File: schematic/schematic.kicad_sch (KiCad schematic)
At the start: 19 parts, among them Q3 2N7000, SW1 PAIRING, U1 MCP4161-xxxx-P, U2 MCP4161-xxxx-P, U3 ESP32-WROOM-32E, U4 MCP4161-xxxx-P, U5 MCP4161-xxxx-P, U6 74HCT245

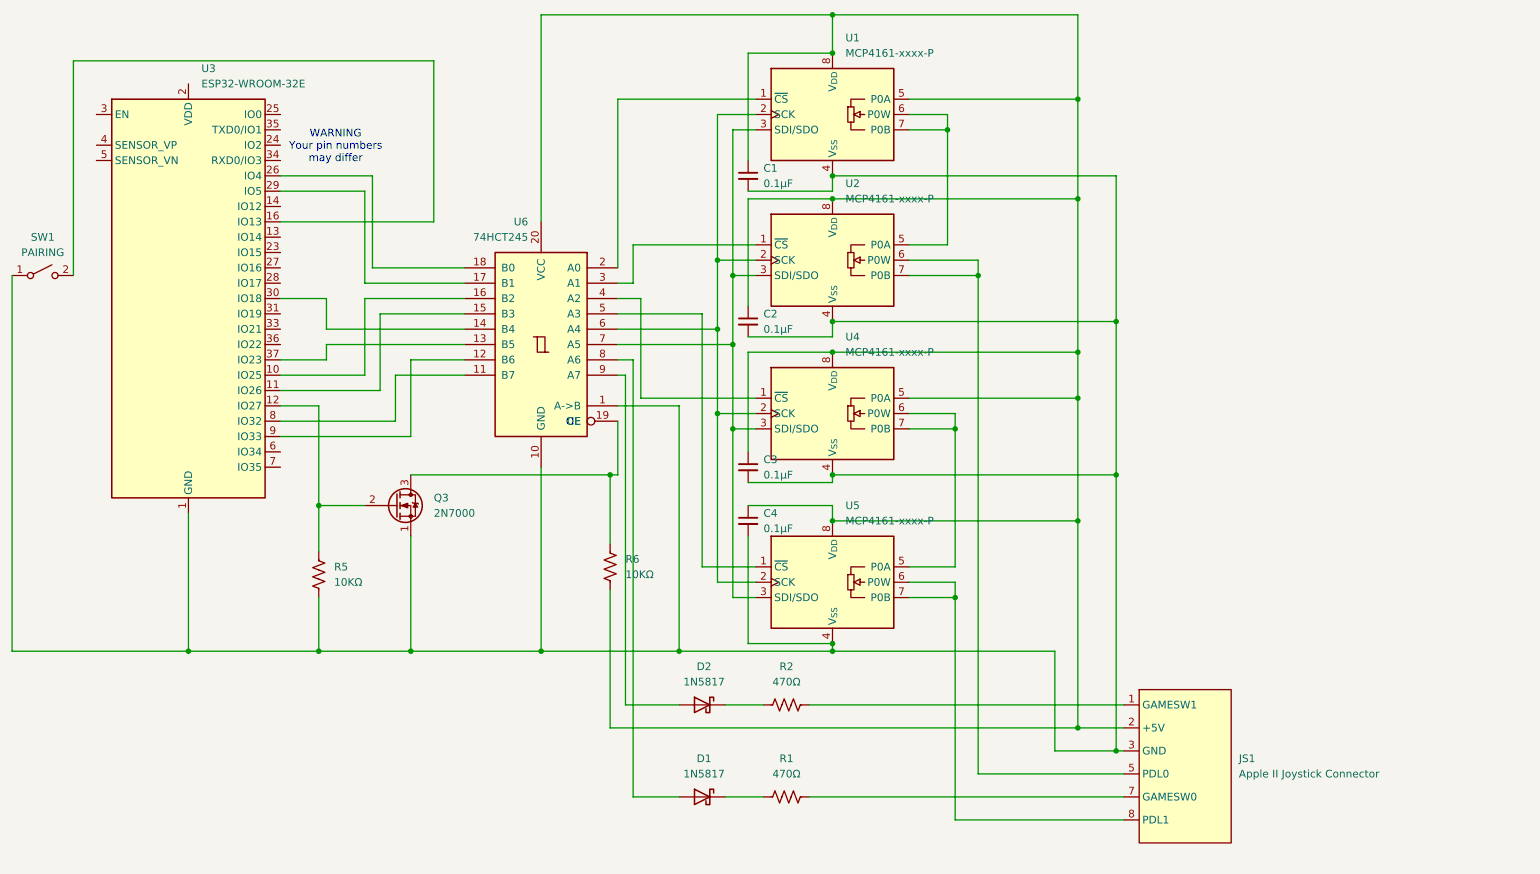
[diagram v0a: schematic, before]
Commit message: pcb first draft
minor changes to the schematic: DE9 connector symbol, the 2 separate diodes changed to one component
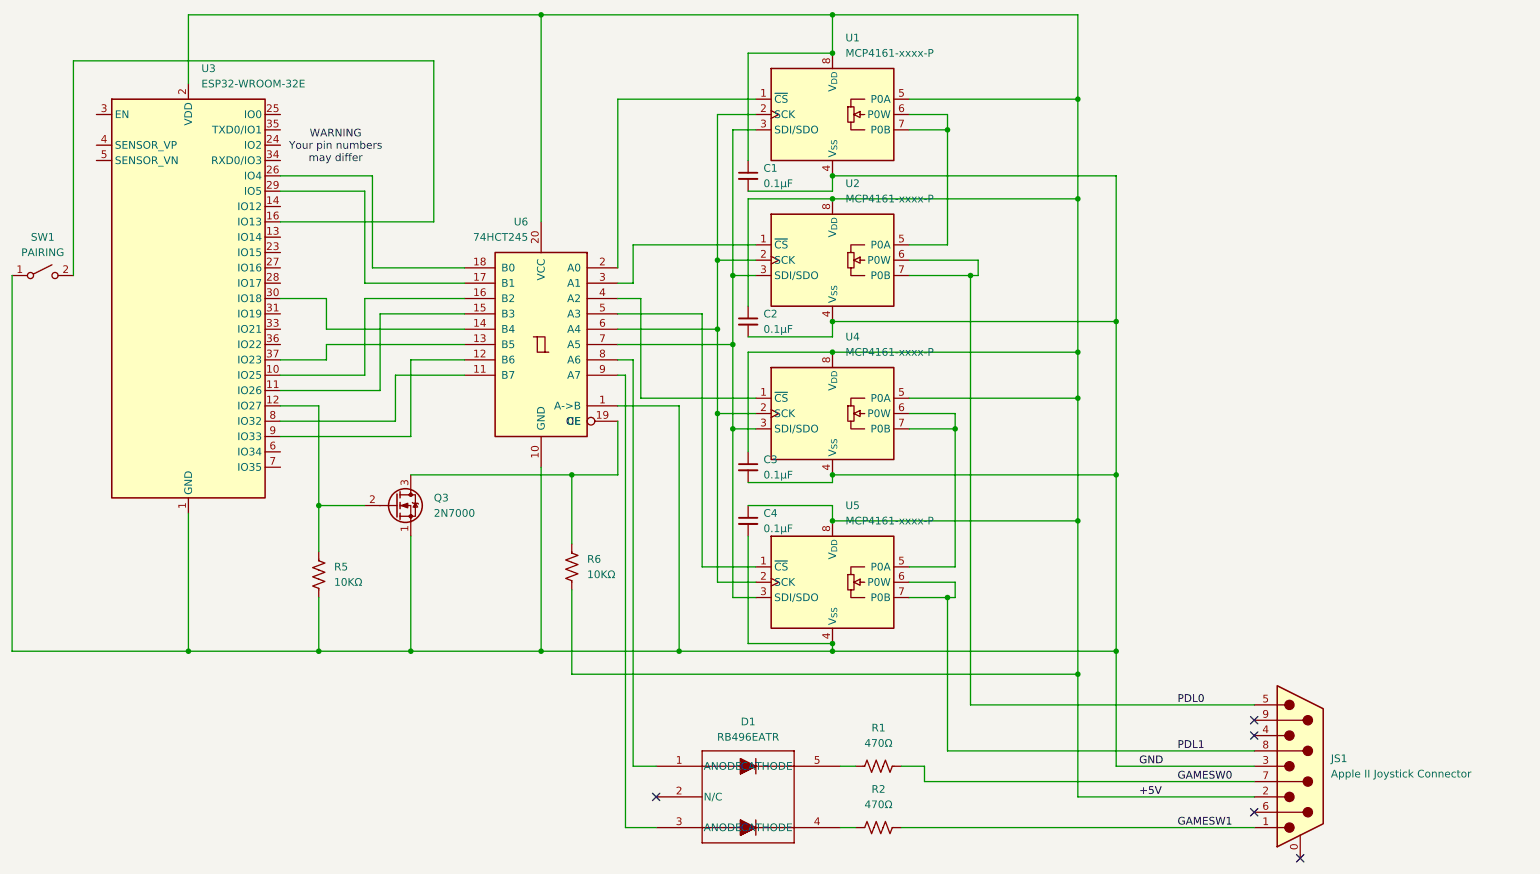
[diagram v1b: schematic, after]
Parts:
- removed D1, D2: 1N5817, Diode_THT:D_DO-41_SOD81_P10.16mm_Horizontal, symbol Diode:1N5817
- removed JS1: Apple II Joystick Connector, symbol kicadlib:AppleIIJoystick
- added D1: RB496EATR, RB496EATR:DIO_FTZ_ROM, symbol RB496EATR:RB496EATR
- added JS1: Apple II Joystick Connector, Connector_Dsub:DSUB-9_Pins_Horizontal_P2.77x2.54mm_EdgePinOffset9.40mm, symbol Connector:DE9_Pins_MountingHoles
- C1, C2, C3, C4: footprint (none) -> Capacitor_SMD:C_0603_1608Metric_Pad1.08x0.95mm_HandSolder
- R1, R2, R5, R6: footprint (none) -> Resistor_SMD:R_0603_1608Metric_Pad0.98x0.95mm_HandSolder
- SW1: footprint (none) -> B3U_1000P_B:B3U-1000P-B
- U1, U2, U4, U5: footprint Package_DIP:DIP-8_W7.62mm -> MCP4161_104E_MS:MSOP8_MC_MCH
- U6: footprint (none) -> SN74HCT245DW:DW20
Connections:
- net GND: now reaches C1.2, C2.2, C3.2, C4.2, Q3.1 (S), R5.2, SW1.1 (A), U1.4 (V_{SS}), U2.4 (V_{SS}), U3.1 (GND), U3.15 (GND), U3.38 (GND), U3.39 (GND), U4.4 (V_{SS}), U5.4 (V_{SS}), U6.1 (A->B), U6.10 (GND)
- net GND: now also JS1.3
- net at R1.1: now also D1.5 (CATHODE)
- net at U6.8 (A6): now also D1.1 (ANODE)
- net +5V: now reaches C1.1, C2.1, C3.1, C4.1, R6.2, U1.5 (P0A), U1.8 (V_{DD}), U2.8 (V_{DD}), U4.5 (P0A), U4.8 (V_{DD}), U5.8 (V_{DD}), U6.20 (VCC)
- net +5V: now also U3.2 (VDD), JS1.2
- net at U6.9 (A7): now also D1.3 (ANODE)
- net GAMESW0: now reaches R1.2
- net GAMESW0: now also JS1.7
- net at R2.1: now also D1.4 (CATHODE)
- net GAMESW1: now reaches R2.2
- net GAMESW1: now also JS1.1
- net PDL0: now reaches U2.6 (P0W), U2.7 (P0B)
- net PDL0: now also JS1.5
- net PDL1: now reaches U5.6 (P0W), U5.7 (P0B)
- net PDL1: now also JS1.8
- no-connect marks 0 -> 5
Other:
- moved on the sheet: R1, R2, R6

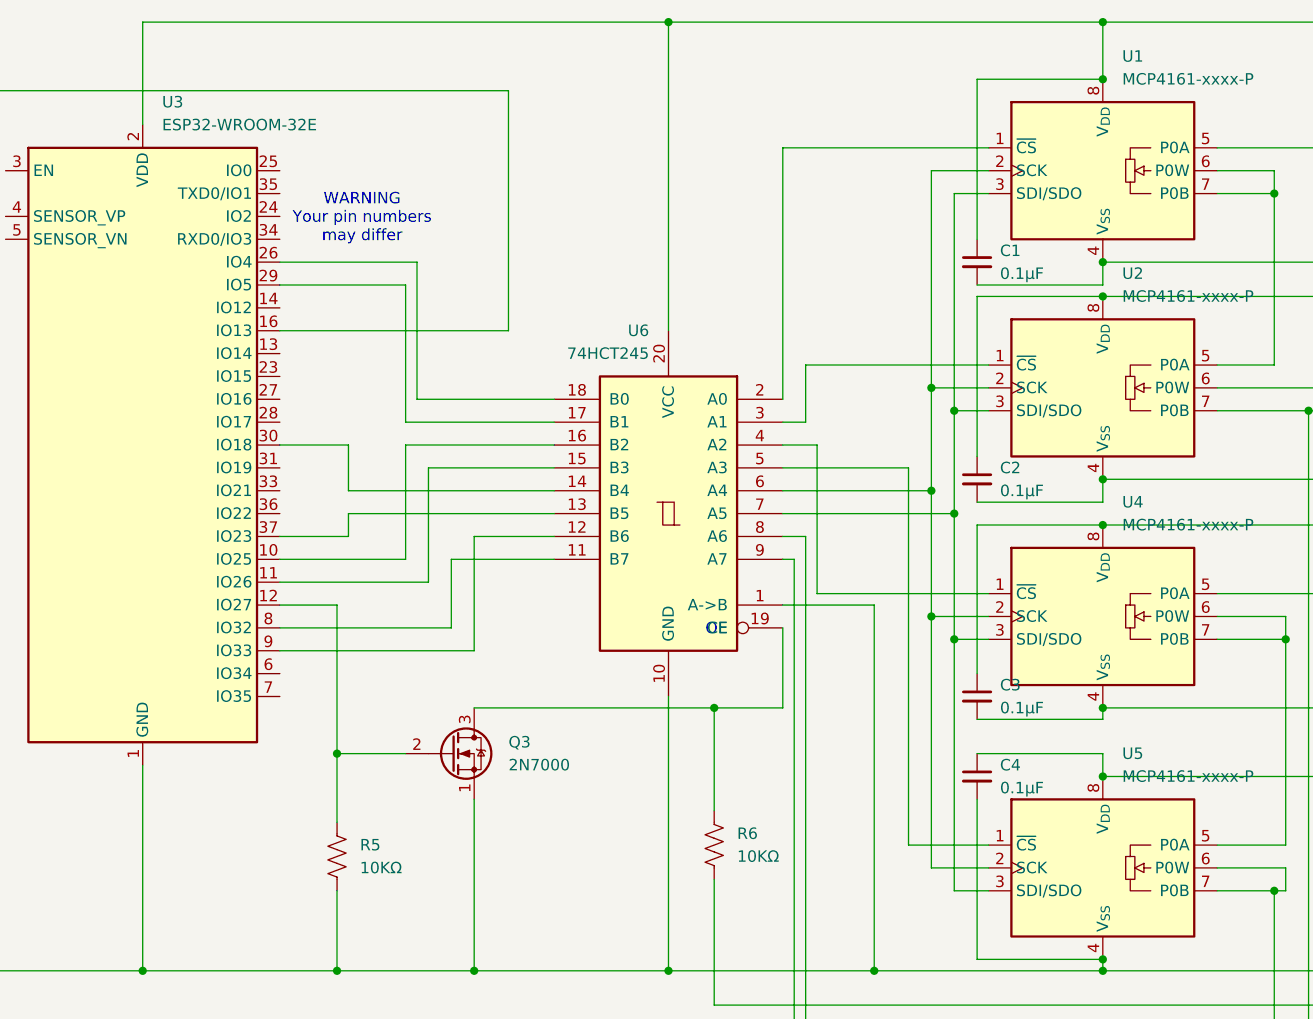
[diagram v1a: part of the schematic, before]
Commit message: maybe fixed caps, made space for de9 jackscrews
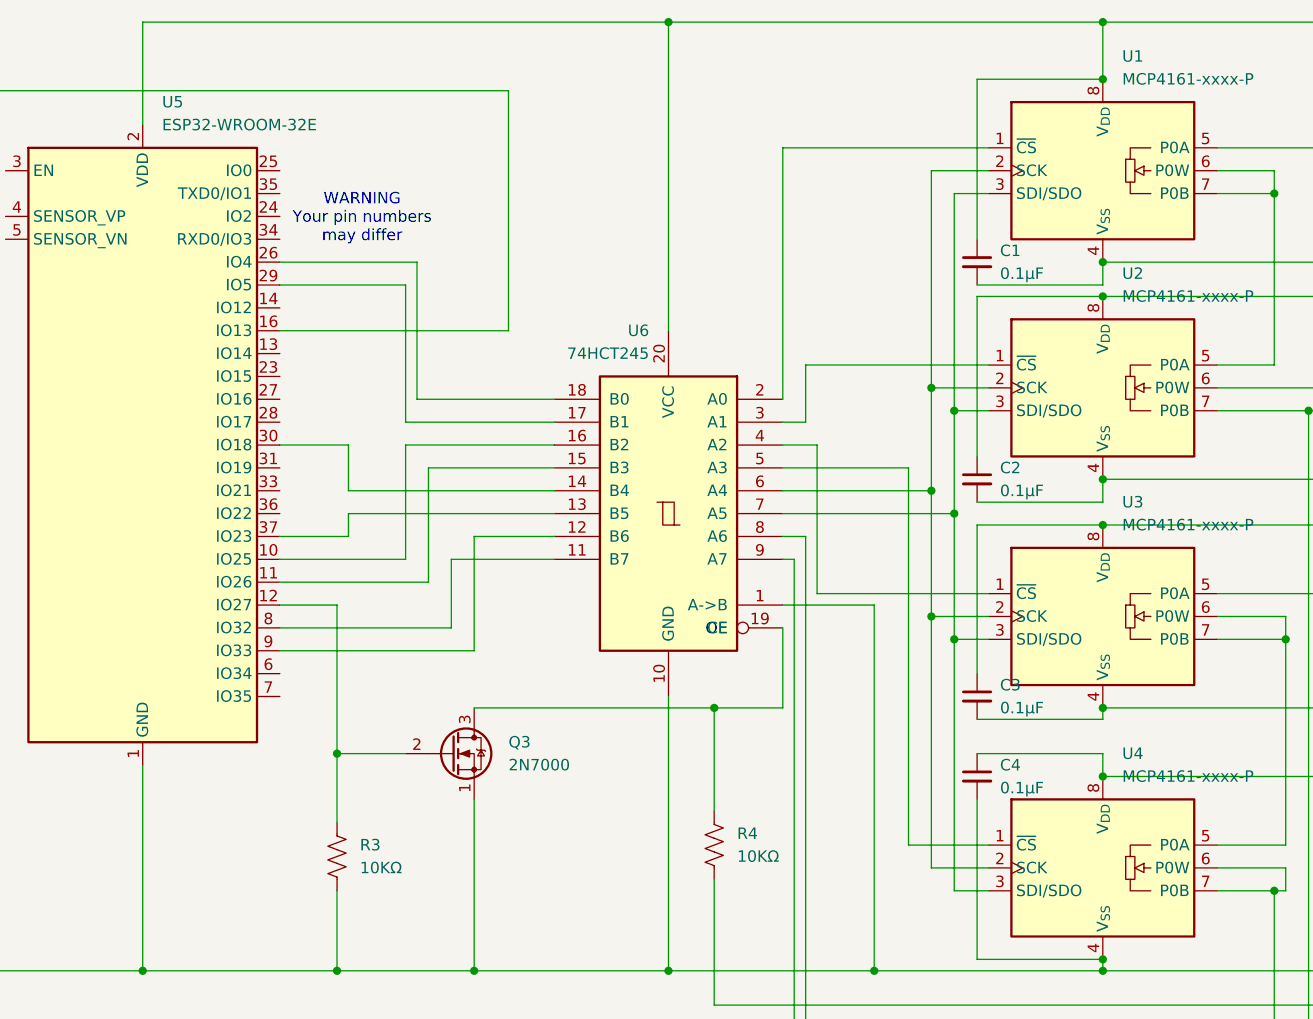
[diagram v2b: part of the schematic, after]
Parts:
- renumbered R5 to R3, R6 to R4, U4 to U3, U5 to U4, U3 to U5
